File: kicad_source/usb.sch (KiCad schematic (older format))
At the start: 18 parts, among them CN4 10118192-0001LF, Q2 BC847, U4 FT230XS

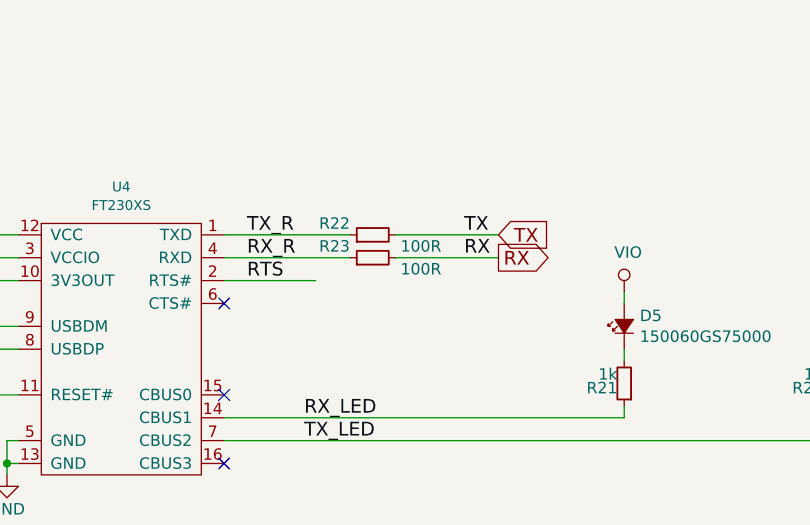
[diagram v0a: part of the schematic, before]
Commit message: exchanged rx and tx of usb serial
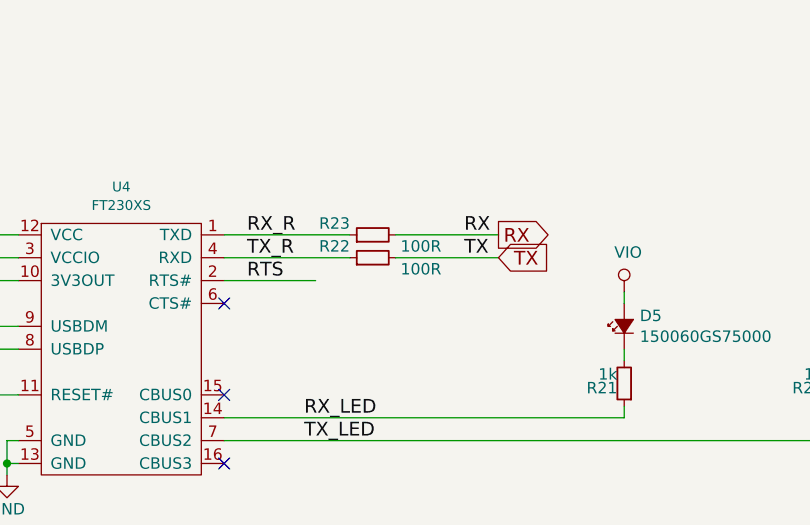
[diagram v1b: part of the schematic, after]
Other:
- moved on the sheet: R22, R23
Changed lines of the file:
@@
 	8200 3100 8200 3150
 Wire Wire Line
+	7000 2450 6450 2450
+Wire Wire Line
 	7000 2350 6450 2350
-Wire Wire Line
-	7000 2450 6450 2450
+Text Label 6550 2450 0    60   ~ 0
+TX_R
 Text Label 6550 2350 0    60   ~ 0
-TX_R
-Text Label 6550 2450 0    60   ~ 0
 RX_R
 $Comp
 L devices:R_1206 R?
 U 1 1 5CB4799A
-P 7100 2350
+P 7100 2450
 AR Path="/5CB4799A" Ref="R?"  Part="1"
 AR Path="/5CB34EF4/5CB4799A" Ref="R?"  Part="1"
 AR Path="/5EB35E34/5CB4799A" Ref="R22"  Part="1"
-F 0 "R22" V 7150 2450 50  0000 L CNN
+F 0 "R22" V 7150 2550 50  0000 L CNN
+F 1 "100R" V 7050 2150 50  0000 L CNN
+F 2 "resistors:R_0603" H 7100 2300 50  0001 C CNN
+F 3 "" H 7100 2450 50  0000 C CNN
+	1    7100 2450
+	0    -1   -1   0
+$EndComp
+$Comp
+L devices:R_1206 R?
+U 1 1 5CB479A1
+P 7100 2350
+AR Path="/5CB479A1" Ref="R?"  Part="1"
+AR Path="/5CB34EF4/5CB479A1" Ref="R?"  Part="1"
+AR Path="/5EB35E34/5CB479A1" Ref="R23"  Part="1"
+F 0 "R23" V 7150 2450 50  0000 L CNN
 F 1 "100R" V 7050 2050 50  0000 L CNN
 F 2 "resistors:R_0603" H 7100 2200 50  0001 C CNN
@@
 	0    -1   -1   0
 $EndComp
-$Comp
-L devices:R_1206 R?
-U 1 1 5CB479A1
-P 7100 2450
-AR Path="/5CB479A1" Ref="R?"  Part="1"
-AR Path="/5CB34EF4/5CB479A1" Ref="R?"  Part="1"
-AR Path="/5EB35E34/5CB479A1" Ref="R23"  Part="1"
-F 0 "R23" V 7150 2550 50  0000 L CNN
-F 1 "100R" V 7050 2150 50  0000 L CNN
-F 2 "resistors:R_0603" H 7100 2300 50  0001 C CNN
-F 3 "" H 7100 2450 50  0000 C CNN
-	1    7100 2450
-	0    -1   -1   0
-$EndComp
+Wire Wire Line
+	7650 2350 7200 2350
 Wire Wire Line
 	7650 2450 7200 2450
-Wire Wire Line
-	7650 2350 7200 2350
+Text Label 7500 2450 0    60   ~ 0
+TX
 Text Label 7500 2350 0    60   ~ 0
-TX
-Text Label 7500 2450 0    60   ~ 0
 RX
-Text GLabel 7650 2450 2    60   Output ~ 0
+Text GLabel 7650 2350 2    60   Output ~ 0
 RX
-Text GLabel 7650 2350 2    60   Input ~ 0
+Text GLabel 7650 2450 2    60   Input ~ 0
 TX
 $Comp

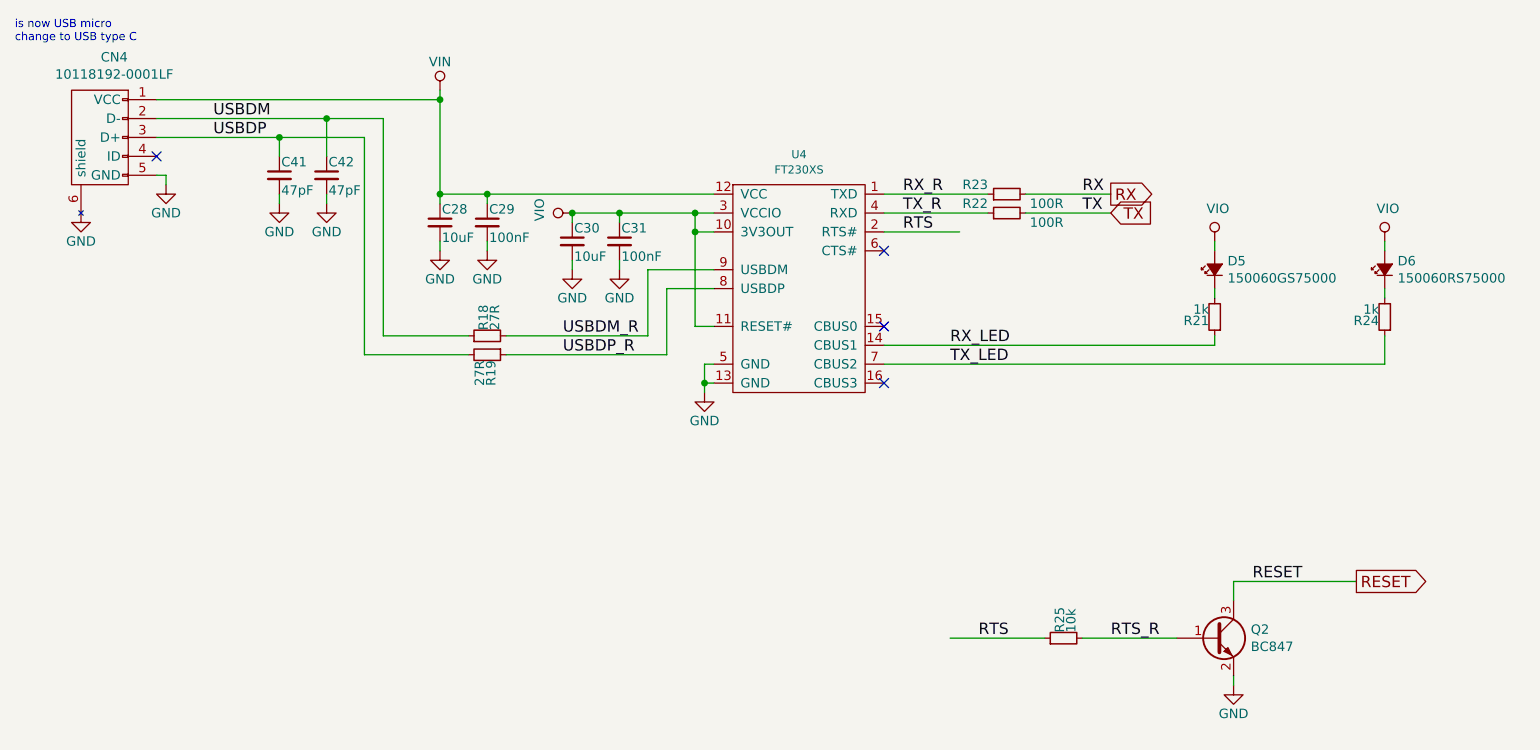
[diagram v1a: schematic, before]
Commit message: reworked reset circuit at usb serial
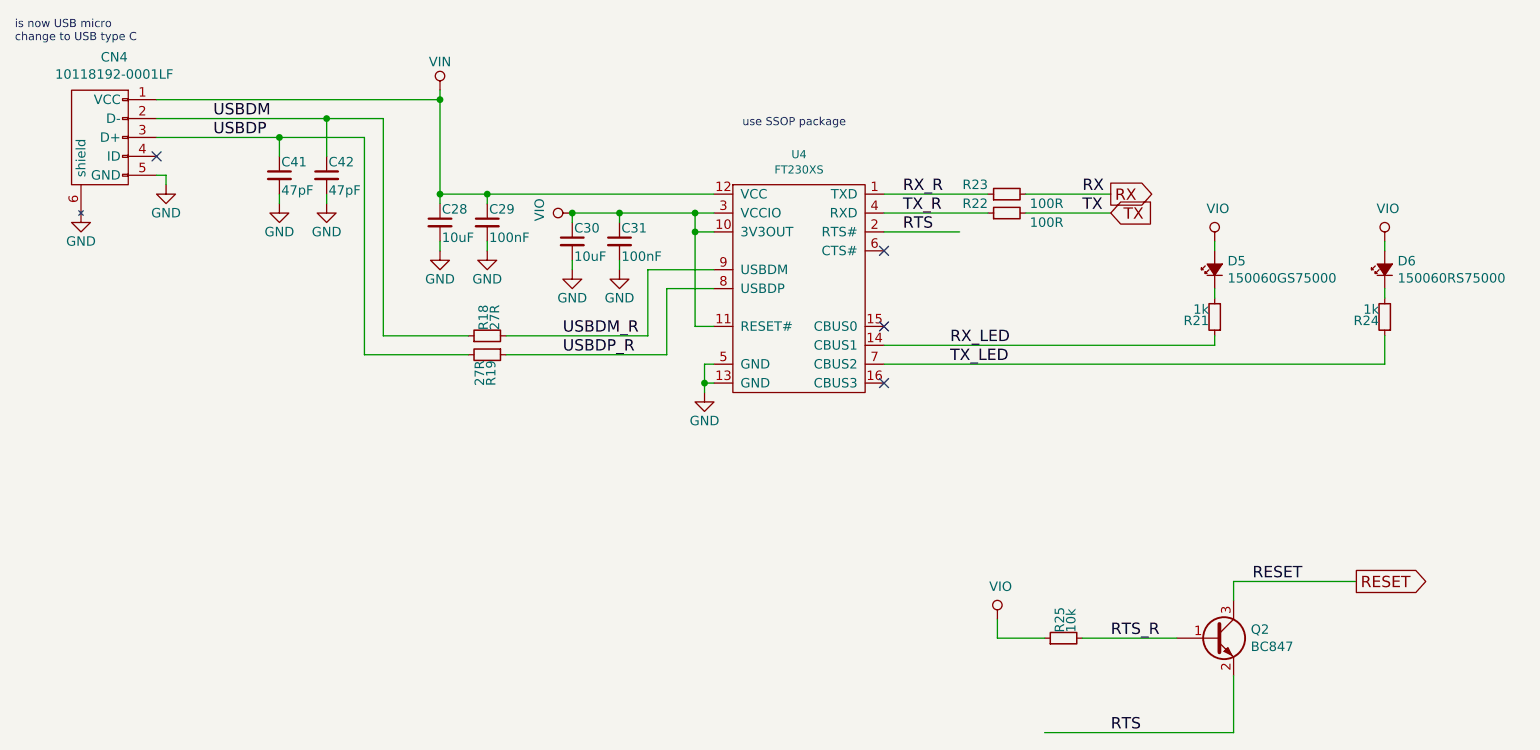
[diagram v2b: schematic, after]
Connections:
- wire segments 62 -> 64
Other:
- note added: "use SSOP package"
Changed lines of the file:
@@
 Wire Wire Line
 	7500 4700 8000 4700
-Text Label 6950 4700 0    60   ~ 0
+Text Label 7650 5200 0    60   ~ 0
 RTS
 Text Label 7650 4700 0    60   ~ 0
@@
 NoConn ~ 6450 3350
 Wire Wire Line
-	6800 4700 7300 4700
-$Comp
-L power-supply:GND #PWR?
-U 1 1 5EC2403C
-P 8300 4950
-AR Path="/5EC2403C" Ref="#PWR?"  Part="1"
-AR Path="/5CB34EF4/5EC2403C" Ref="#PWR?"  Part="1"
-AR Path="/5EB35E34/5EC2403C" Ref="#PWR086"  Part="1"
-F 0 "#PWR086" H 8300 4700 50  0001 C CNN
-F 1 "GND" H 8300 4800 50  0000 C CNN
-F 2 "" H 8300 4950 50  0000 C CNN
-F 3 "" H 8300 4950 50  0000 C CNN
-	1    8300 4950
-	1    0    0    -1
-$EndComp
-Wire Wire Line
-	8300 4900 8300 4950
-Wire Wire Line
 	9100 3250 9100 3100
 Wire Wire Line
@@
 Wire Wire Line
 	8200 2850 8200 2900
+Text Notes 5700 2000 0    43   ~ 0
+use SSOP package
+Wire Wire Line
+	7300 5200 8300 5200
+Wire Wire Line
+	8300 4900 8300 5200
+$Comp
+L power-supply:VIO #PWR?
+U 1 1 5EFEC333
+P 7050 4600
+AR Path="/5EFEC333" Ref="#PWR?"  Part="1"
+AR Path="/5CB34EF4/5EFEC333" Ref="#PWR?"  Part="1"
+AR Path="/5EB35E34/5EFEC333" Ref="#PWR0102"  Part="1"
+F 0 "#PWR0102" H 7050 4450 50  0001 C CNN
+F 1 "VIO" H 7067 4773 50  0000 C CNN
+F 2 "" H 7050 4600 50  0000 C CNN
+F 3 "" H 7050 4600 50  0000 C CNN
+	1    7050 4600
+	1    0    0    -1
+$EndComp
+Wire Wire Line
+	7050 4600 7050 4700
+Wire Wire Line
+	7050 4700 7300 4700
 $EndSCHEMATC
